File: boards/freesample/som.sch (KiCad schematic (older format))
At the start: 0 parts

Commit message: Continued work on schematic capture
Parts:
- added C129, C130, C131, C132: 0.1 uF, symbol device:C
- added J7: CONN_INTEGRALSTICK_FPGA_HOST, symbol special-azonenberg:CONN_INTEGRALSTICK_FPGA_HOST
- added J8: CONN_INTEGRALSTICK_MCU_HOST, symbol special-azonenberg:CONN_INTEGRALSTICK_MCU_HOST
- added J9: 0826-1G1T-23-F, symbol special-azonenberg:BEL_FUSE_0826-1G1T-23-F
- added R16, R17: 470, symbol device:R
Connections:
- new net: J7.100 (3V3), J7.105 (3V3), J7.106 (3V3), J7.111 (3V3), J7.112 (3V3), J7.117 (3V3), J7.118 (3V3), J7.69 (3V3), J7.70 (3V3), J7.75 (3V3), J7.76 (3V3), J7.81 (3V3), J7.82 (3V3), J7.87 (3V3), J7.88 (3V3), J7.93 (3V3), J7.94 (3V3), J7.99 (3V3)
- new net: J7.13 (2V5), J7.14 (2V5), J7.19 (2V5), J7.20 (2V5), J7.25 (2V5), J7.26 (2V5), J7.31 (2V5), J7.32 (2V5), J7.37 (2V5), J7.38 (2V5), J7.7 (2V5), J7.8 (2V5)
- new net: J7.39 (1V8), J7.40 (1V8), J7.45 (1V8), J7.46 (1V8), J7.51 (1V8), J7.52 (1V8), J7.57 (1V8), J7.58 (1V8), J7.63 (1V8), J7.64 (1V8)
- new net: J8.1 (3V3), J8.103 (3V3), J8.104 (3V3), J8.109 (3V3), J8.110 (3V3), J8.115 (3V3), J8.116 (3V3), J8.13 (3V3), J8.19 (3V3), J8.25 (3V3), J8.31 (3V3), J8.32 (3V3), J8.37 (3V3), J8.38 (3V3), J8.43 (3V3), J8.44 (3V3), J8.49 (3V3), J8.50 (3V3), J8.55 (3V3), J8.56 (3V3), J8.61 (3V3), J8.62 (3V3), J8.67 (3V3), J8.68 (3V3), J8.7 (3V3), J8.73 (3V3), J8.74 (3V3), J8.79 (3V3), J8.80 (3V3), J8.85 (3V3), J8.86 (3V3), J8.91 (3V3), J8.92 (3V3), J8.97 (3V3), J8.98 (3V3)
- new net: J9.14 (LED1_P), R16.1
- new net: J9.16 (LED2_P), R17.1
- new net 5V0: J7.1 (5V0), J7.2 (5V0), J7.3 (5V0), J7.4 (5V0), J7.5 (5V0), J7.6 (5V0)
- new net ETH_A_N: J8.6 (ETH_A_N), J9.10 (CH1_N)
- new net ETH_A_P: J8.4 (ETH_A_P), J9.11 (CH1_P)
- new net ETH_A_TAP: C129.2, J9.12 (CH1_TAP)
- new net ETH_B_N: J8.12 (ETH_B_N), J9.5 (CH2_N)
- new net ETH_B_P: J8.10 (ETH_B_P), J9.4 (CH2_P)
- new net ETH_B_TAP: C130.2, J9.6 (CH2_TAP)
- new net ETH_C_N: J8.18 (ETH_C_N), J9.2 (CH3_N)
- new net ETH_C_P: J8.16 (ETH_C_P), J9.3 (CH3_P)
- new net ETH_C_TAP: C131.2, J9.1 (CH3_TAP)
- new net ETH_D_N: J8.24 (ETH_D_N), J9.9 (CH4_N)
- new net ETH_D_P: J8.22 (ETH_D_P), J9.8 (CH4_P)
- new net ETH_D_TAP: C132.2, J9.7 (CH4_TAP)
- new net ETH_LED1_P: R16.2
- new net ETH_LED2_P: R17.2
- new net GND: C129.1, C130.1, C131.1, C132.1, J7.121 (GND), J7.122 (GND), J7.123 (GND), J7.124 (GND), J7.125 (GND), J7.126 (GND), J7.127 (GND), J7.128 (GND), J8.121 (GND), J8.122 (GND), J8.123 (GND), J8.124 (GND), J8.125 (GND), J8.126 (GND), J8.127 (GND), J8.128 (GND), J8.14 (GND), J8.2 (GND), J8.20 (GND), J8.26 (GND), J8.8 (GND), J9.13 (LED1_N), J9.15 (LED2_N)

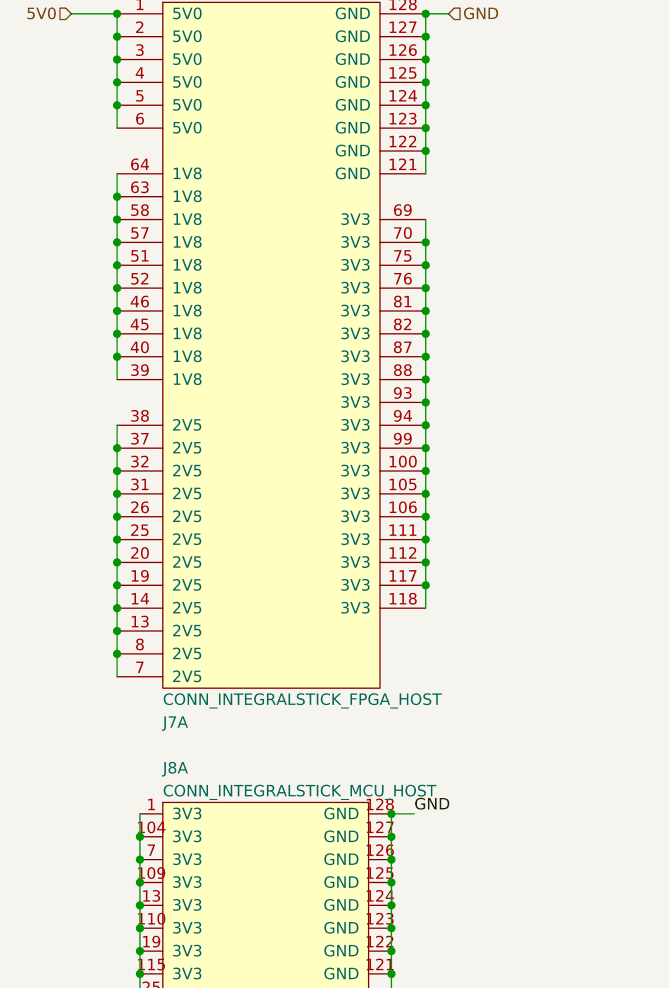
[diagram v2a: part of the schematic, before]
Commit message: Continued work on FREESAMPLE schematic including PSU.
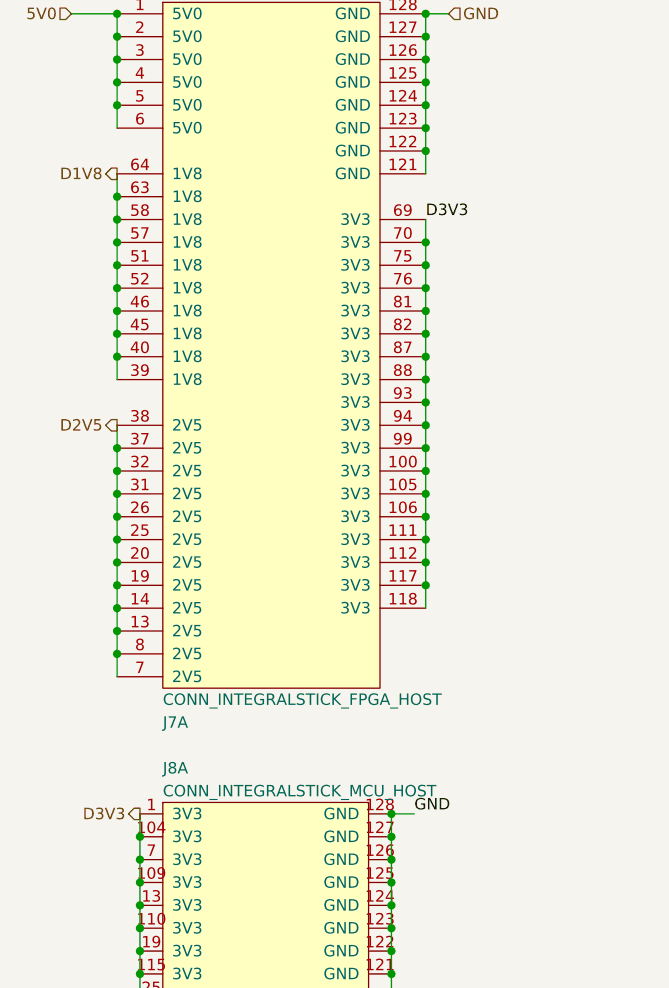
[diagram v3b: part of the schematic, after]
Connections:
- net D3V3: now reaches J7.100 (3V3), J7.105 (3V3), J7.106 (3V3), J7.111 (3V3), J7.112 (3V3), J7.117 (3V3), J7.118 (3V3), J7.69 (3V3), J7.70 (3V3), J7.75 (3V3), J7.76 (3V3), J7.81 (3V3), J7.82 (3V3), J7.87 (3V3), J7.88 (3V3), J7.93 (3V3), J7.94 (3V3), J7.99 (3V3)
- net D3V3: now also J8.1 (3V3), J8.103 (3V3), J8.104 (3V3), J8.109 (3V3), J8.110 (3V3), J8.115 (3V3), J8.116 (3V3), J8.13 (3V3), J8.19 (3V3), J8.25 (3V3), J8.31 (3V3), J8.32 (3V3), J8.37 (3V3), J8.38 (3V3), J8.43 (3V3), J8.44 (3V3), J8.49 (3V3), J8.50 (3V3), J8.55 (3V3), J8.56 (3V3), J8.61 (3V3), J8.62 (3V3), J8.67 (3V3), J8.68 (3V3), J8.7 (3V3), J8.73 (3V3), J8.74 (3V3), J8.79 (3V3), J8.80 (3V3), J8.85 (3V3), J8.86 (3V3), J8.91 (3V3), J8.92 (3V3), J8.97 (3V3), J8.98 (3V3)
- net D2V5: now reaches J7.13 (2V5), J7.14 (2V5), J7.19 (2V5), J7.20 (2V5), J7.25 (2V5), J7.26 (2V5), J7.31 (2V5), J7.32 (2V5), J7.37 (2V5), J7.38 (2V5), J7.7 (2V5), J7.8 (2V5)
- net D1V8: now reaches J7.39 (1V8), J7.40 (1V8), J7.45 (1V8), J7.46 (1V8), J7.51 (1V8), J7.52 (1V8), J7.57 (1V8), J7.58 (1V8), J7.63 (1V8), J7.64 (1V8)
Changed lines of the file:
@@
 Sheet 9 12
 Title "FREESAMPLE Oscilloscope"
-Date "2018-12-17"
+Date "2019-02-23"
 Rev "0.1"
 Comp "Andrew D. Zonenberg / Antikernel Labs"
@@
 Wire Wire Line
 	1100 7550 1100 7450
+Text HLabel 1100 4250 0    50   Output ~ 0
+D3V3
+Text HLabel 1000 2550 0    50   Output ~ 0
+D2V5
+Text HLabel 1000 1450 0    50   Output ~ 0
+D1V8
+Text Label 2350 1650 0    50   ~ 0
+D3V3
 $EndSCHEMATC

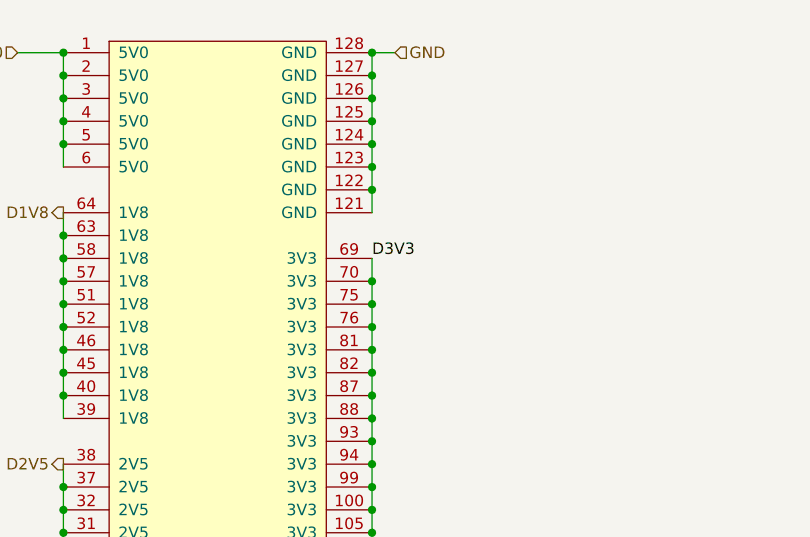
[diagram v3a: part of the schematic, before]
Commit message: Hooked up new power rails
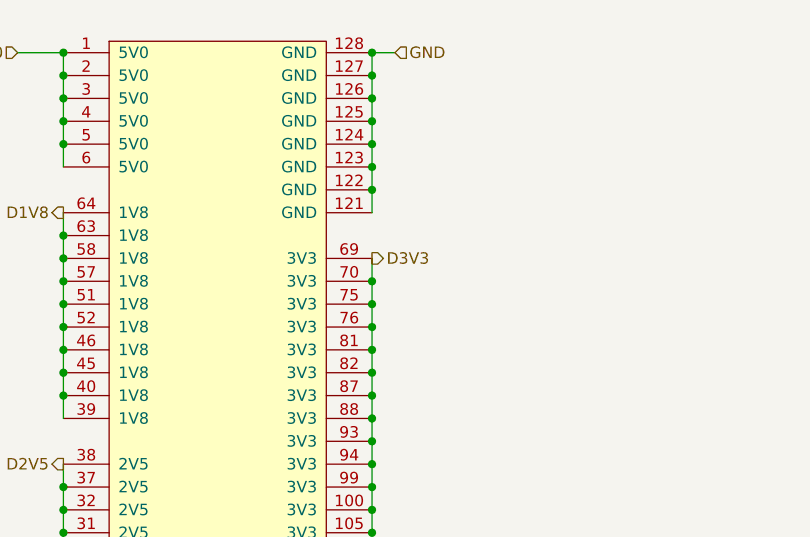
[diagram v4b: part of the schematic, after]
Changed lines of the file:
@@
 Sheet 9 12
 Title "FREESAMPLE Oscilloscope"
-Date "2019-02-23"
+Date "2019-02-26"
 Rev "0.1"
 Comp "Andrew D. Zonenberg / Antikernel Labs"
@@
 Text HLabel 1000 1450 0    50   Output ~ 0
 D1V8
-Text Label 2350 1650 0    50   ~ 0
+Text HLabel 2350 1650 2    50   Output ~ 0
 D3V3
 $EndSCHEMATC

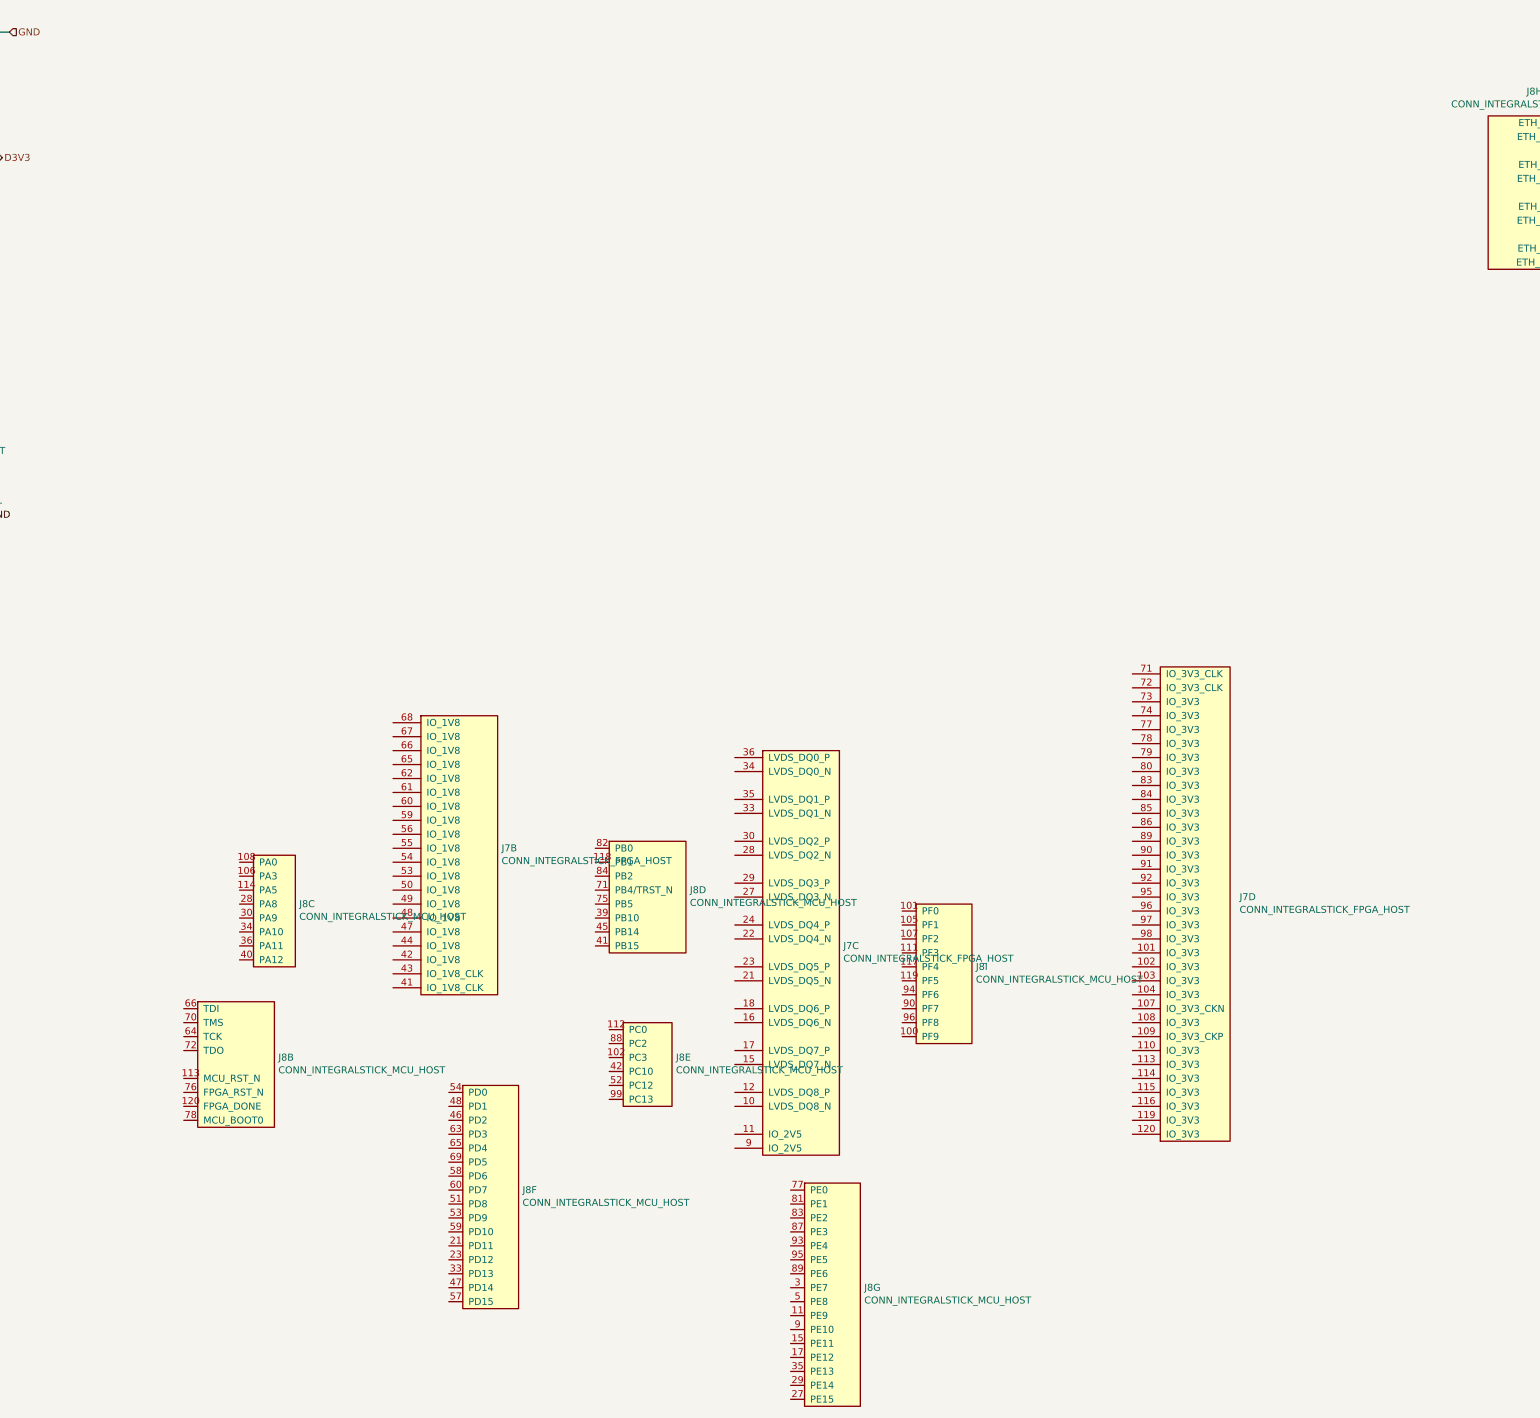
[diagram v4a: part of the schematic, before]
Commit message: Continued schematic capture work. Hooked up most SoM connectors.
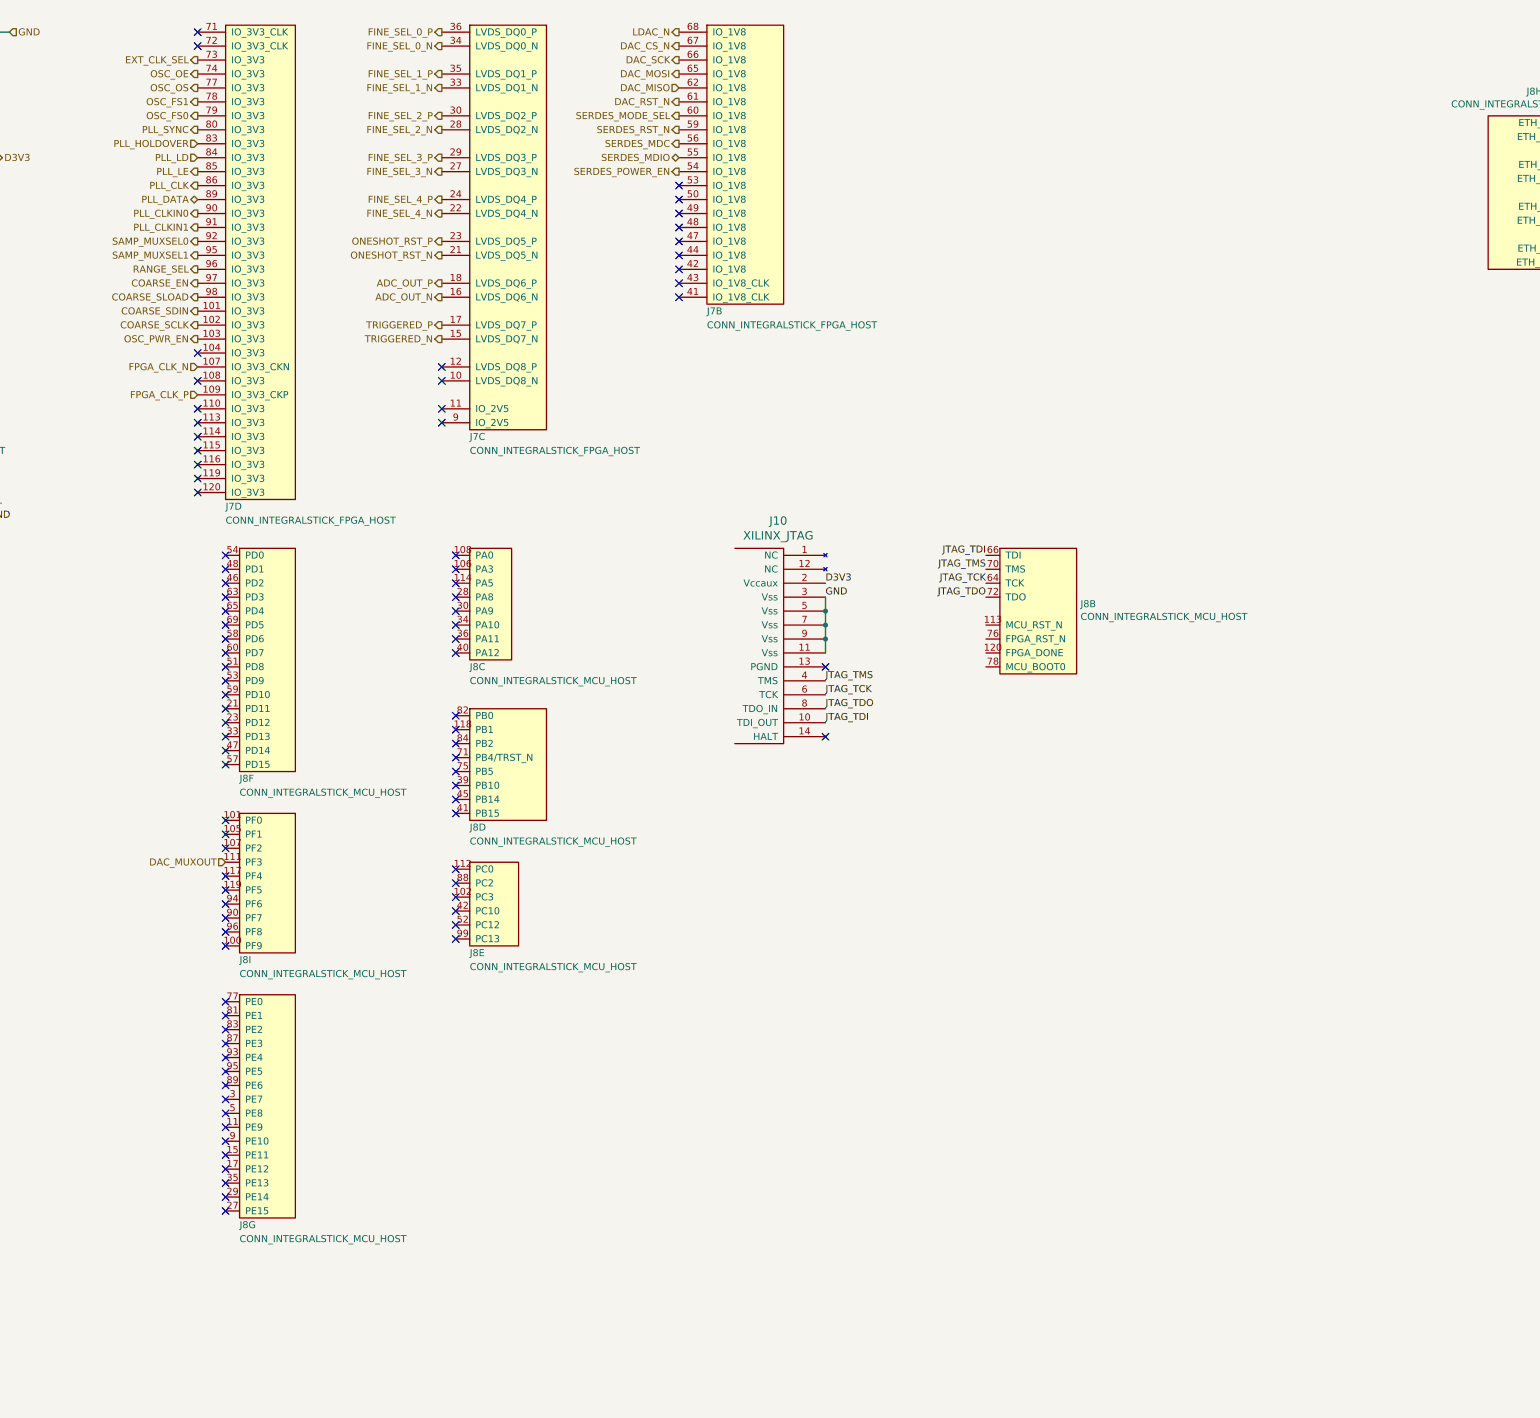
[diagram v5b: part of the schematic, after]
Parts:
- added J10: XILINX_JTAG, symbol xilinx-azonenberg:XILINX_JTAG
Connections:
- net D3V3: now also J10.2 (Vccaux)
- net GND: now also J10.11 (Vss), J10.3 (Vss), J10.5 (Vss), J10.7 (Vss), J10.9 (Vss)
- net SERDES_POWER_EN: now reaches J7.54 (IO_1V8)
- net SERDES_MDIO: now reaches J7.55 (IO_1V8)
- net SERDES_MDC: now reaches J7.56 (IO_1V8)
- net SERDES_RST_N: now reaches J7.59 (IO_1V8)
- net SERDES_MODE_SEL: now reaches J7.60 (IO_1V8)
- net DAC_RST_N: now reaches J7.61 (IO_1V8)
- net DAC_MISO: now reaches J7.62 (IO_1V8)
- net DAC_MOSI: now reaches J7.65 (IO_1V8)
- net DAC_SCK: now reaches J7.66 (IO_1V8)
- net DAC_CS_N: now reaches J7.67 (IO_1V8)
- net LDAC_N: now reaches J7.68 (IO_1V8)
- net TRIGGERED_N: now reaches J7.15 (LVDS_DQ7_N)
- net ADC_OUT_N: now reaches J7.16 (LVDS_DQ6_N)
- net TRIGGERED_P: now reaches J7.17 (LVDS_DQ7_P)
- net ADC_OUT_P: now reaches J7.18 (LVDS_DQ6_P)
- net ONESHOT_RST_N: now reaches J7.21 (LVDS_DQ5_N)
- net FINE_SEL_4_N: now reaches J7.22 (LVDS_DQ4_N)
- net ONESHOT_RST_P: now reaches J7.23 (LVDS_DQ5_P)
- net FINE_SEL_4_P: now reaches J7.24 (LVDS_DQ4_P)
- net FINE_SEL_3_N: now reaches J7.27 (LVDS_DQ3_N)
- net FINE_SEL_2_N: now reaches J7.28 (LVDS_DQ2_N)
- net FINE_SEL_3_P: now reaches J7.29 (LVDS_DQ3_P)
- net FINE_SEL_2_P: now reaches J7.30 (LVDS_DQ2_P)
- net FINE_SEL_1_N: now reaches J7.33 (LVDS_DQ1_N)
- net FINE_SEL_0_N: now reaches J7.34 (LVDS_DQ0_N)
- net FINE_SEL_1_P: now reaches J7.35 (LVDS_DQ1_P)
- net FINE_SEL_0_P: now reaches J7.36 (LVDS_DQ0_P)
- net COARSE_SDIN: now reaches J7.101 (IO_3V3)
- net COARSE_SCLK: now reaches J7.102 (IO_3V3)
- net OSC_PWR_EN: now reaches J7.103 (IO_3V3)
- net FPGA_CLK_N: now reaches J7.107 (IO_3V3_CKN)
- net FPGA_CLK_P: now reaches J7.109 (IO_3V3_CKP)
- net EXT_CLK_SEL: now reaches J7.73 (IO_3V3)
- net OSC_OE: now reaches J7.74 (IO_3V3)
- net OSC_OS: now reaches J7.77 (IO_3V3)
- net OSC_FS1: now reaches J7.78 (IO_3V3)
- net OSC_FS0: now reaches J7.79 (IO_3V3)
- net PLL_SYNC: now reaches J7.80 (IO_3V3)
- net PLL_HOLDOVER: now reaches J7.83 (IO_3V3)
- net PLL_LD: now reaches J7.84 (IO_3V3)
- net PLL_LE: now reaches J7.85 (IO_3V3)
- net PLL_CLK: now reaches J7.86 (IO_3V3)
- net PLL_DATA: now reaches J7.89 (IO_3V3)
- net PLL_CLKIN0: now reaches J7.90 (IO_3V3)
- net PLL_CLKIN1: now reaches J7.91 (IO_3V3)
- net SAMP_MUXSEL0: now reaches J7.92 (IO_3V3)
- net SAMP_MUXSEL1: now reaches J7.95 (IO_3V3)
- net RANGE_SEL: now reaches J7.96 (IO_3V3)
- net COARSE_EN: now reaches J7.97 (IO_3V3)
- net COARSE_SLOAD: now reaches J7.98 (IO_3V3)
- net JTAG_TCK: now reaches J8.64 (TCK)
- net JTAG_TCK: now also J10.6 (TCK)
- net JTAG_TDI: now reaches J8.66 (TDI)
- net JTAG_TDI: now also J10.10 (TDI_OUT)
- net JTAG_TMS: now reaches J8.70 (TMS)
- net JTAG_TMS: now also J10.4 (TMS)
- net JTAG_TDO: now reaches J8.72 (TDO)
- net JTAG_TDO: now also J10.8 (TDO_IN)
- net DAC_MUXOUT: now reaches J8.111 (PF3)
- no-connect marks 0 -> 89
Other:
- moved on the sheet: J7B, J7C, J7D, J8B, J8C, J8D, J8E, J8F, J8G, J8I

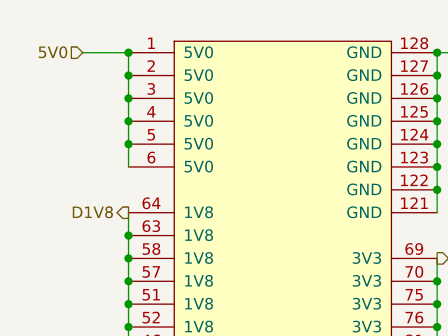
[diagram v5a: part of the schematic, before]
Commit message: Lots of ERC fixes, added CML-to-LVDS buffers for FPGA input signals
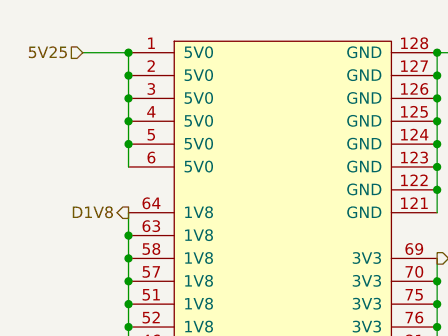
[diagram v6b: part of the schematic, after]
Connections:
- net 5V0 renamed 5V25
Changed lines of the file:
@@
 ETH_D_N
 Text HLabel 800  750  0    50   Input ~ 0
-5V0
+5V25
 Wire Wire Line
 	800  750  1000 750
